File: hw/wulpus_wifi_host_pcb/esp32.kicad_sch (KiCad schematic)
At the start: 1 part, among them U4 XIAO-ESP32-C6-SMD

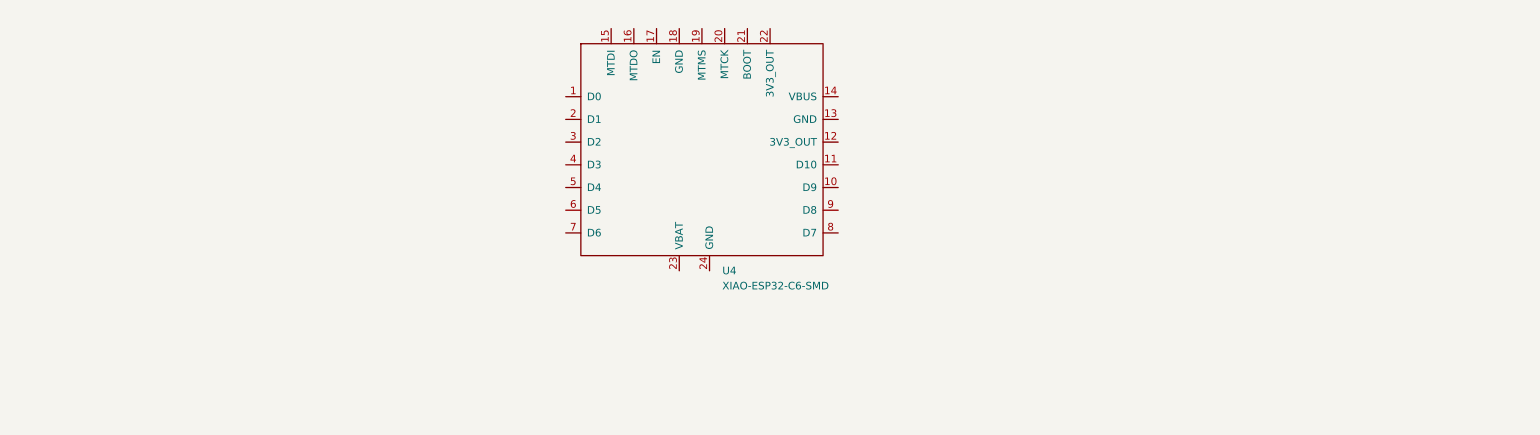
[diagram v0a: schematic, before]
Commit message: Added hierarchical shets, signals for esp32 and battery protector ref schematic
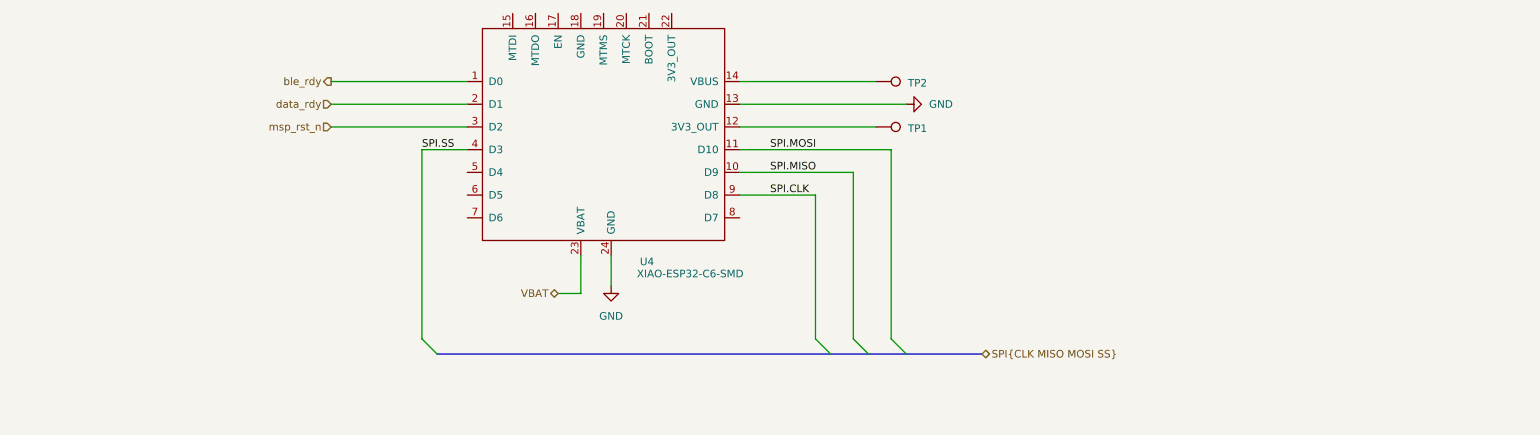
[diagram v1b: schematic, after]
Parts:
- added TP1, TP2: TestPoint, TestPoint:TestPoint_Pad_1.5x1.5mm, symbol Connector:TestPoint
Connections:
- net ble_rdy: now reaches U4.1 (D0)
- net SPI.MISO: now reaches U4.10 (D9)
- net SPI.MOSI: now reaches U4.11 (D10)
- net at U4.12 (3V3_OUT): now also TP1.1
- net GND: now reaches U4.13 (GND)
- net GND: now also U4.24 (GND)
- net at U4.14 (VBUS): now also TP2.1
- net data_rdy: now reaches U4.2 (D1)
- net VBAT: now reaches U4.23 (VBAT)
- net msp_rst_n: now reaches U4.3 (D2)
- net SPI.SS: now reaches U4.4 (D3)
- net SPI.CLK: now reaches U4.9 (D8)
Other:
- moved on the sheet: U4

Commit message: Updated footprints, mapped 3D models, added layerstack, partial placement and layout
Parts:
- removed TP1, TP2: TestPoint, TestPoint:TestPoint_Pad_1.5x1.5mm, symbol Connector:TestPoint
- added R1, R10, R11, R2, R3, R4, R5, R6, R7, R8, R9: 47, Resistor_SMD:R_0402_1005Metric, symbol Device:R
- renumbered U4 to U1
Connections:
- net SPI.CLK: now also R8.2; no longer U1.9 (D8)
- net SPI.MISO: now also R9.2; no longer U1.10 (D9)
- net SPI.MOSI: now also R10.2; no longer U1.11 (D10)
- net SPI.SS: now also R11.2; no longer U1.4 (D3)
- net data_rdy: now also R2.1; no longer U1.2 (D1)
- net +3V3 ESP: now reaches U1.12 (3V3_OUT)
- net VBUS: now reaches U1.14 (VBUS)
- net at U1.5 (D4): now also R5.2
- net at U1.6 (D5): now also R6.2
- net at U1.7 (D6): now also R7.2
- net at U1.8 (D7): now also R11.1
- net ble_rdy: no longer names the net of U1.1 (D0)
- net ble_rdy: now also R1.2
- net msp_rst_n: no longer names the net of U1.3 (D2)
- net msp_rst_n: now also R3.2
- new net: R8.1, U1.11 (D10)
- new net: R10.1, U1.9 (D8)
- new net: R2.2, U1.2 (D1)
- new net: R4.2, U1.4 (D3)
- new net: R9.1, U1.10 (D9)
- new net MSP_JTAG.RST_n: R1.1
- new net MSP_JTAG.TCK: R7.1
- new net MSP_JTAG.TDI: R5.1
- new net MSP_JTAG.TDO: R4.1
- new net MSP_JTAG.TEST: R3.1
- new net MSP_JTAG.TMS: R6.1
- no-connect marks 0 -> 8
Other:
- moved on the sheet: U1

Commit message: Changed cap footprints to 0603
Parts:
- U1: MANUFACTURER (none) -> Seeed Studio; MP (none) -> XIAO ESP32C6
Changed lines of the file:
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@@
+			)
+		)
+		(property "MP" " XIAO ESP32C6"
+			(at 152.4 99.06 0)
+			(hide yes)
+			(show_name no)
+			(do_not_autoplace no)
+			(effects
+				(font
+					(size 1.27 1.27)
+				)
+			)
+		)
+		(property "MANUFACTURER" "Seeed Studio"
+			(at 152.4 99.06 0)
+			(hide yes)
+			(show_name no)
+			(do_not_autoplace no)
+			(effects
+				(font
+					(size 1.27 1.27)
+				)
 			)
 		)

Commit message: Fixed BOM, added jobset file, regenerated fabrication outputs
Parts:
- R1, R10, R11, R2, R3, R4, R5, R6, R7, R8, R9: MANUFACTURER (none) -> Yageo; MP (none) -> RC0402FR-1347RL

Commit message: Rename project to WULPUS Pro Max
- update user-facing branding across documentation, firmware, and software
- update repository URLs while preserving compatibility identifiers
- release WiFi host PCB v1.0.1 with revised metadata and silkscreen
- regenerate hardware design and fabrication outputs
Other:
- title: (none) -> WULPUS Pro Max WiFi host
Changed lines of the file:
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@@
 	(generator_version "10.0")
 	(paper "A4")
+	(title_block
+		(title "WULPUS Pro Max WiFi host")
+		(rev "v1.0.1")
+		(comment 1 "Reviewer: Cedric Hirschi")
+		(comment 2 "Author: Sergei Vostrikov")
+	)
 	(text_box "Software-emulated JTAG interface is used to programm MSP430 MCU from ESP32"
 		(exclude_from_sim no)
